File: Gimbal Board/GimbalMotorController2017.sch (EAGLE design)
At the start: 124 parts, among them J1 SL03THROUGH_HOLE, J3 APP_2POS_CONFIG5V_HORIZ, Q7 MOSFET-PCHANNEL, Q8 MOSFET-PCHANNEL, Q9 MOSFET-NCHANNELAO3404A, U1 NUP4201MR6, U2 MAX3232D, U3 CSD18533Q5A, U4 CSD18533Q5A, U5 CSD18533Q5A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

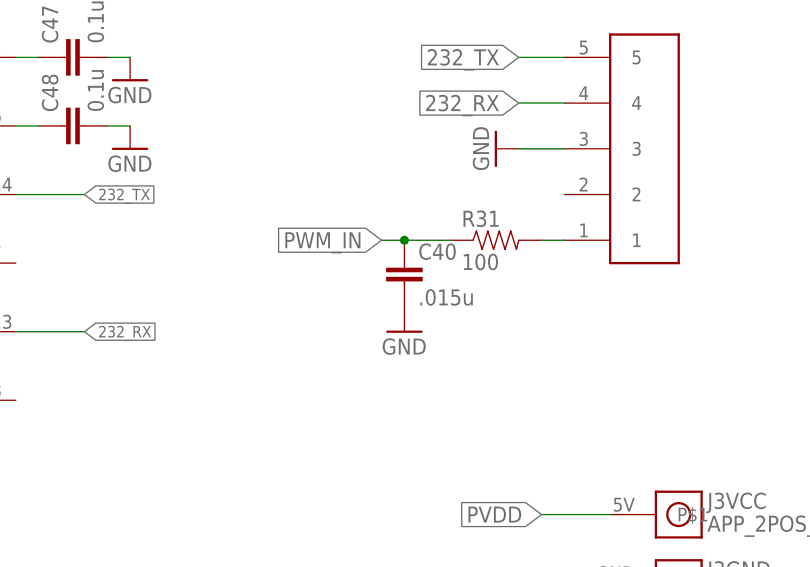
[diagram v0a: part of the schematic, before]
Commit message: Forgot to include the schematic for the board
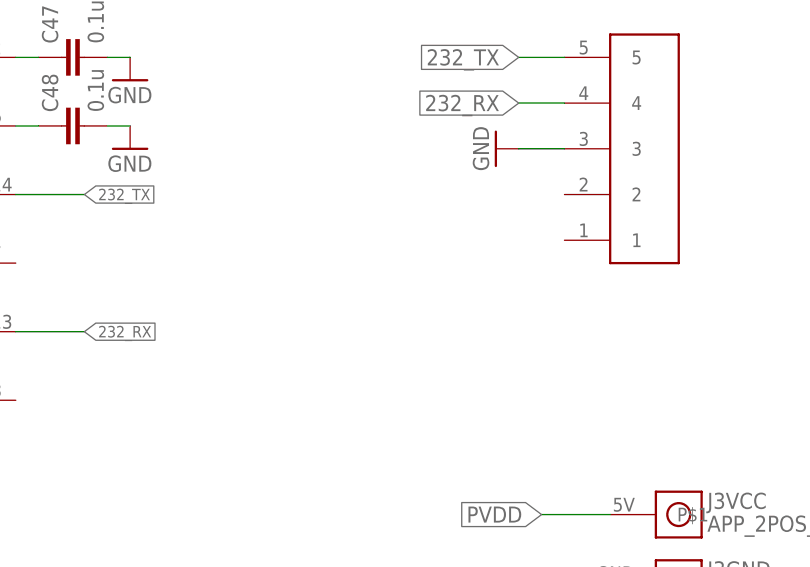
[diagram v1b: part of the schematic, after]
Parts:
- removed C40: .015u, SparkFun-Passives:CAP0805
- removed R31: 100, SparkFun-Passives:RESISTOR0805-RES
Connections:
- removed net N$34: R31.2, U$4.1
- net GND: no longer C40.2
- net PWM_IN: no longer C40.1, R31.1
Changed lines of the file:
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@@
 <part name="SH1" library="BLDC_Motor_Controller_2016_Rev1" deviceset="SHORT-H" device="T5"/>
 <part name="SH2" library="BLDC_Motor_Controller_2016_Rev1" deviceset="SHORT-H" device="T5"/>
-<part name="R31" library="SparkFun-Passives" deviceset="RESISTOR" device="0805-RES" value="100"/>
-<part name="C40" library="SparkFun-Passives" deviceset="CAP" device="0805" value=".015u"/>
-<part name="GND34" library="SparkFun-Aesthetics" deviceset="GND" device=""/>
 <part name="Q9" library="SparkFun-DiscreteSemi" deviceset="MOSFET-NCHANNEL" device="AO3404A"/>
 <part name="R51" library="SparkFun-Passives" deviceset="RESISTOR" device="0805-RES" value="1M"/>
@@
 <instance part="SH1" gate="G$1" x="101.6" y="-66.04"/>
 <instance part="SH2" gate="G$1" x="101.6" y="25.4"/>
-<instance part="R31" gate="G$1" x="309.88" y="-73.66"/>
-<instance part="C40" gate="G$1" x="299.72" y="-78.74"/>
-<instance part="GND34" gate="1" x="299.72" y="-83.82"/>
 <instance part="Q9" gate="G$1" x="-33.02" y="-121.92"/>
 <instance part="R51" gate="G$1" x="-45.72" y="-129.54" rot="R270"/>
@@
 </segment>
 <segment>
-<pinref part="C40" gate="G$1" pin="2"/>
-<pinref part="GND34" gate="1" pin="GND"/>
-</segment>
-<segment>
 <pinref part="R51" gate="G$1" pin="2"/>
 <pinref part="GND35" gate="1" pin="GND"/>
@@
 <net name="PWM_IN" class="0">
 <segment>
-<pinref part="C40" gate="G$1" pin="1"/>
-<wire x1="299.72" y1="-73.66" x2="304.8" y2="-73.66" width="0.1524" layer="91"/>
-<pinref part="R31" gate="G$1" pin="1"/>
-<wire x1="299.72" y1="-73.66" x2="297.18" y2="-73.66" width="0.1524" layer="91"/>
-<junction x="299.72" y="-73.66"/>
-<label x="297.18" y="-73.66" size="1.778" layer="95" rot="R180" xref="yes"/>
-</segment>
-<segment>
 <pinref part="U$2" gate="G$1" pin="PA2"/>
 <wire x1="269.24" y1="71.12" x2="261.62" y2="71.12" width="0.1524" layer="91"/>
@@
 </segment>
 </net>
-<net name="N$34" class="0">
-<segment>
-<pinref part="R31" gate="G$1" pin="2"/>
-<pinref part="U$4" gate="G$1" pin="1"/>
-<wire x1="317.5" y1="-73.66" x2="314.96" y2="-73.66" width="0.1524" layer="91"/>
-</segment>
-</net>
